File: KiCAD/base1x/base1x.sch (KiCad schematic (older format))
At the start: 41 parts, among them J1 Conn_02x05_Odd_Even, J2 GS3, J3 Conn_02x14_Counter_Clockwise, J4 GS3, J5 Screw_Terminal_01x06, J6 Conn_02x14_Counter_Clockwise, J7 Conn_02x06_Counter_Clockwise, J8 Conn_02x06_Counter_Clockwise, J9 Screw_Terminal_01x08, P1 CONN_01X02, P2 CONN_01X02, P3 CONN_01X02, P4 CONN_01X02, U1 ADS1115

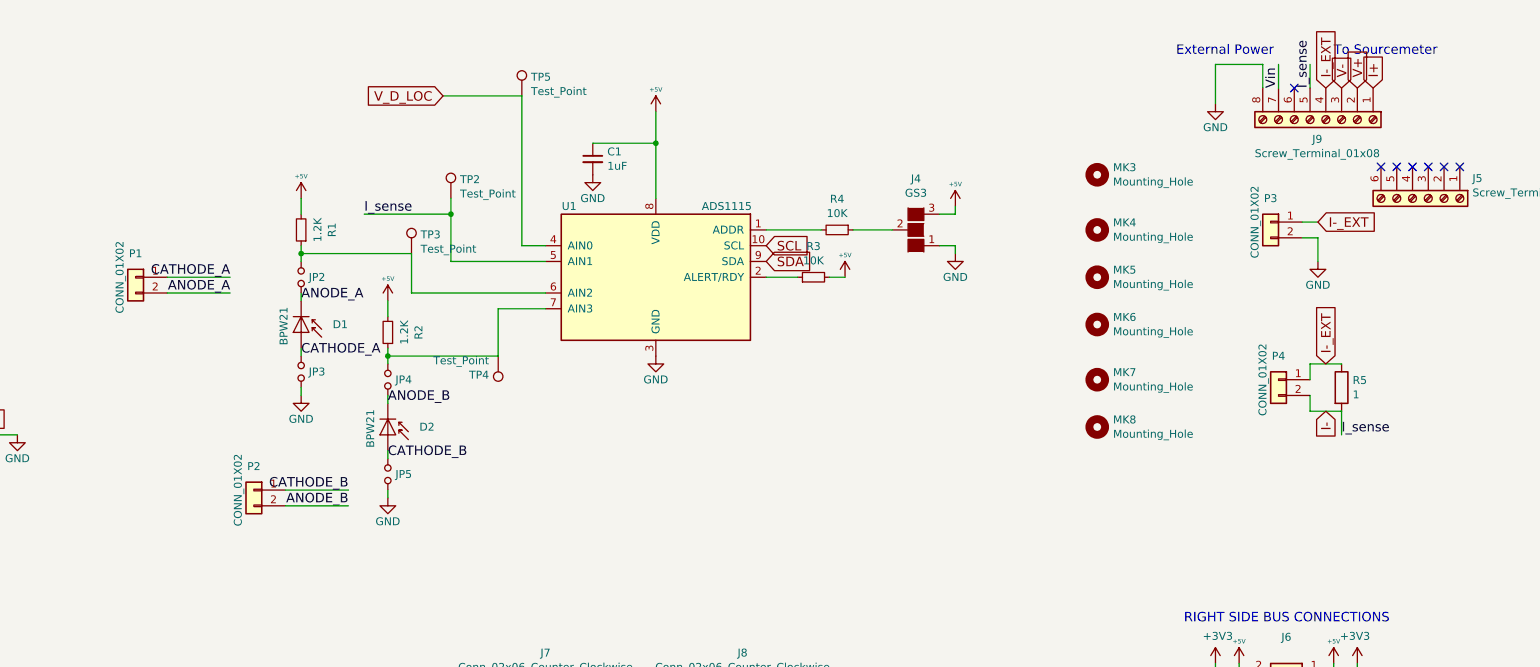
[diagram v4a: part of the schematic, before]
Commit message: rotate connectors on newMux
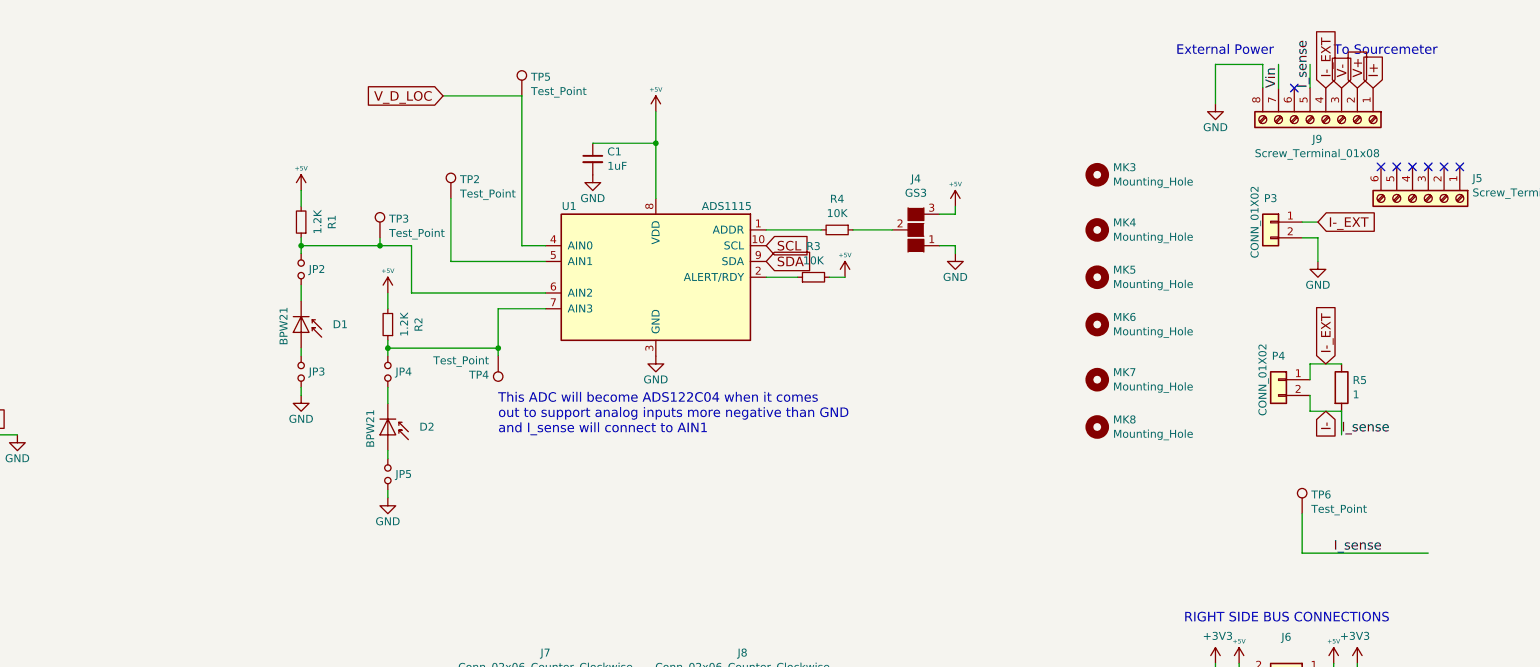
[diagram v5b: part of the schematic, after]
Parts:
- removed P1, P2: CONN_01X02, Pin_Headers:Pin_Header_Straight_1x02_Pitch2.54mm, symbol Conn_01x02
- added TP6: Test_Point, myParts:Test_Point_S1751-46R, symbol Test_Point
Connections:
- net I-: now also TP6.1; no longer TP2.1, U1.5 (AIN1)
- net ANODE_A: no longer names the net of D1.1 (K), JP2.2
- net ANODE_B: no longer names the net of D2.1 (K), JP4.2
- net CATHODE_A: no longer names the net of D1.2 (A), JP3.1
- net CATHODE_B: no longer names the net of D2.2 (A), JP5.1
- new net: TP2.1, U1.5 (AIN1)
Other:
- note added: "This ADC will become ADS122C04 when it comes\nout to support analog inputs more negative than GND\nand I_sense will connect to AIN1"
- moved on the sheet: JP2, JP4, R1, R2, TP3
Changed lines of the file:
@@
 $EndComp
 Wire Wire Line
-	6000 1850 6000 1300
+	6000 1300 6000 1850
 $Comp
 L C_Small C1
@@
 L +5V #PWR013
 U 1 1 59F74573
-P 3750 1850
-F 0 "#PWR013" H 3750 1700 50  0001 C CNN
-F 1 "+5V" H 3750 1990 28  0000 C CNN
-F 2 "" H 3750 1850 50  0000 C CNN
-F 3 "" H 3750 1850 50  0000 C CNN
-	1    3750 1850
+P 3750 1800
+F 0 "#PWR013" H 3750 1650 50  0001 C CNN
+F 1 "+5V" H 3750 1940 28  0000 C CNN
+F 2 "" H 3750 1800 50  0000 C CNN
+F 3 "" H 3750 1800 50  0000 C CNN
+	1    3750 1800
 	1    0    0    -1
 $EndComp
@@
 	1    0    0    -1
 $EndComp
-Text Label 3750 2500 0    60   ~ 0
-ANODE_A
-Text Label 3750 2850 0    60   ~ 0
-CATHODE_A
-$Comp
-L Conn_01x02 P1
-U 1 1 59F745A3
-P 2700 2350
-F 0 "P1" H 2700 2500 50  0000 C CNN
-F 1 "CONN_01X02" V 2800 2350 50  0000 C CNN
-F 2 "Pin_Headers:Pin_Header_Straight_1x02_Pitch2.54mm" H 2700 2350 50  0001 C CNN
-F 3 "" H 2700 2350 50  0000 C CNN
-	1    2700 2350
-	-1   0    0    -1
-$EndComp
-Text Label 3300 2450 2    60   ~ 0
-ANODE_A
-Text Label 3300 2350 2    60   ~ 0
-CATHODE_A
-Wire Wire Line
-	3750 1850 3750 1950
-Wire Wire Line
-	2900 2350 3300 2350
-Wire Wire Line
-	2900 2450 3300 2450
+Wire Wire Line
+	3750 1800 3750 1900
 $Comp
 L R_Small R1
 U 1 1 59F761B7
-P 3750 2050
-F 0 "R1" V 3554 2050 50  0000 C CNN
-F 1 "1.2K" V 3645 2050 50  0000 C CNN
-F 2 "Resistors_SMD:R_0805_HandSoldering" H 3750 2050 50  0001 C CNN
-F 3 "" H 3750 2050 50  0001 C CNN
-	1    3750 2050
+P 3750 2000
+F 0 "R1" V 3554 2000 50  0000 C CNN
+F 1 "1.2K" V 3645 2000 50  0000 C CNN
+F 2 "Resistors_SMD:R_0805_HandSoldering" H 3750 2000 50  0001 C CNN
+F 3 "" H 3750 2000 50  0001 C CNN
+	1    3750 2000
 	-1   0    0    1
 $EndComp
 Wire Wire Line
-	4450 2200 4450 2450
+	4450 2150 4450 2450
 Wire Wire Line
 	4450 2450 5300 2450
@@
 L Jumper_NO_Small JP2
 U 1 1 59F7708F
-P 3750 2350
-F 0 "JP2" V 3750 2398 50  0000 L CNN
-F 1 "Jumper_NO_Small" V 3795 2398 50  0001 L CNN
-F 2 "Connectors:GS2" H 3750 2350 50  0001 C CNN
-F 3 "" H 3750 2350 50  0001 C CNN
-	1    3750 2350
-	0    1    1    0
-$EndComp
-Wire Wire Line
-	3750 2450 3750 2500
-Wire Wire Line
-	3750 2150 3750 2250
-Wire Wire Line
-	4450 2200 3750 2200
-Connection ~ 3750 2200
+P 3750 2300
+F 0 "JP2" V 3750 2348 50  0000 L CNN
+F 1 "Jumper_NO_Small" V 3795 2348 50  0001 L CNN
+F 2 "Connectors:GS2" H 3750 2300 50  0001 C CNN
+F 3 "" H 3750 2300 50  0001 C CNN
+	1    3750 2300
+	0    1    1    0
+$EndComp
+Wire Wire Line
+	3750 2400 3750 2500
+Wire Wire Line
+	3750 2100 3750 2200
+Wire Wire Line
+	4450 2150 3750 2150
+Connection ~ 3750 2150
 $Comp
 L Jumper_NO_Small JP3
@@
 L +5V #PWR016
 U 1 1 59F77B25
-P 4300 2500
-F 0 "#PWR016" H 4300 2350 50  0001 C CNN
-F 1 "+5V" H 4300 2640 28  0000 C CNN
-F 2 "" H 4300 2500 50  0000 C CNN
-F 3 "" H 4300 2500 50  0000 C CNN
-	1    4300 2500
+P 4300 2450
+F 0 "#PWR016" H 4300 2300 50  0001 C CNN
+F 1 "+5V" H 4300 2590 28  0000 C CNN
+F 2 "" H 4300 2450 50  0000 C CNN
+F 3 "" H 4300 2450 50  0000 C CNN
+	1    4300 2450
 	1    0    0    -1
 $EndComp
@@
 	1    0    0    -1
 $EndComp
-Text Label 4300 3150 0    60   ~ 0
-ANODE_B
-Text Label 4300 3500 0    60   ~ 0
-CATHODE_B
-Wire Wire Line
-	4300 2500 4300 2600
+Wire Wire Line
+	4300 2450 4300 2550
 $Comp
 L R_Small R2
 U 1 1 59F77B34
-P 4300 2700
-F 0 "R2" V 4104 2700 50  0000 C CNN
-F 1 "1.2K" V 4195 2700 50  0000 C CNN
-F 2 "Resistors_SMD:R_0805_HandSoldering" H 4300 2700 50  0001 C CNN
-F 3 "" H 4300 2700 50  0001 C CNN
-	1    4300 2700
+P 4300 2650
+F 0 "R2" V 4104 2650 50  0000 C CNN
+F 1 "1.2K" V 4195 2650 50  0000 C CNN
+F 2 "Resistors_SMD:R_0805_HandSoldering" H 4300 2650 50  0001 C CNN
+F 3 "" H 4300 2650 50  0001 C CNN
+	1    4300 2650
 	-1   0    0    1
 $EndComp
@@
 L Jumper_NO_Small JP4
 U 1 1 59F77B3B
-P 4300 3000
-F 0 "JP4" V 4300 3048 50  0000 L CNN
-F 1 "Jumper_NO_Small" V 4345 3048 50  0001 L CNN
-F 2 "Connectors:GS2" H 4300 3000 50  0001 C CNN
-F 3 "" H 4300 3000 50  0001 C CNN
-	1    4300 3000
-	0    1    1    0
-$EndComp
-Wire Wire Line
-	4300 3100 4300 3150
-Wire Wire Line
-	4300 2800 4300 2900
-Wire Wire Line
-	5000 2850 4300 2850
-Connection ~ 4300 2850
-$Comp
-L Jumper_NO_Small JP5
-U 1 1 59F77B46
-P 4300 3600
-F 0 "JP5" V 4300 3648 50  0000 L CNN
-F 1 "Jumper_NO_Small" V 4345 3648 50  0001 L CNN
-F 2 "Connectors:GS2" H 4300 3600 50  0001 C CNN
-F 3 "" H 4300 3600 50  0001 C CNN
-	1    4300 3600
-	0    1    1    0
-$EndComp
+P 4300 2950
+F 0 "JP4" V 4300 2998 50  0000 L CNN
+F 1 "Jumper_NO_Small" V 4345 2998 50  0001 L CNN
+F 2 "Connectors:GS2" H 4300 2950 50  0001 C CNN
+F 3 "" H 4300 2950 50  0001 C CNN
+	1    4300 2950
+	0    1    1    0
+$EndComp
+Wire Wire Line
+	4300 3050 4300 3150
+Wire Wire Line
+	4300 2750 4300 2850
+Wire Wire Line
+	5000 2800 4300 2800
+Connection ~ 4300 2800
 Wire Wire Line
 	4300 3450 4300 3500
@@
 	4300 3700 4300 3750
 Wire Wire Line
-	5000 2850 5000 2550
+	5000 2550 5000 2850
 Wire Wire Line
 	5000 2550 5300 2550
-$Comp
-L Conn_01x02 P2
-U 1 1 59F77FAB
-P 3450 3700
-F 0 "P2" H 3450 3850 50  0000 C CNN
-F 1 "CONN_01X02" V 3550 3700 50  0000 C CNN
-F 2 "Pin_Headers:Pin_Header_Straight_1x02_Pitch2.54mm" H 3450 3700 50  0001 C CNN
-F 3 "" H 3450 3700 50  0000 C CNN
-	1    3450 3700
-	-1   0    0    -1
-$EndComp
-Text Label 4050 3800 2    60   ~ 0
-ANODE_B
-Text Label 4050 3700 2    60   ~ 0
-CATHODE_B
-Wire Wire Line
-	3650 3700 4050 3700
-Wire Wire Line
-	3650 3800 4050 3800
 $Comp
 L GS3 J2
@@
 L Test_Point TP3
 U 1 1 5A3700D5
-P 4450 2200
-F 0 "TP3" H 4508 2320 50  0000 L CNN
-F 1 "Test_Point" H 4508 2229 50  0000 L CNN
-F 2 "myParts:Test_Point_S1751-46R" H 4650 2200 50  0001 C CNN
-F 3 "" H 4650 2200 50  0001 C CNN
-	1    4450 2200
+P 4250 2100
+F 0 "TP3" H 4308 2220 50  0000 L CNN
+F 1 "Test_Point" H 4308 2129 50  0000 L CNN
+F 2 "myParts:Test_Point_S1751-46R" H 4450 2100 50  0001 C CNN
+F 3 "" H 4450 2100 50  0001 C CNN
+	1    4250 2100
 	1    0    0    -1
 $EndComp
@@
 	-1   0    0    1
 $EndComp
-Wire Wire Line
-	4700 1950 4150 1950
-Connection ~ 4700 1950
-Text Label 4150 1950 0    60   ~ 0
-I_sense
 Text GLabel 4650 1200 0    60   Input ~ 0
 V_D_LOC
@@
 	1    0    0    -1
 $EndComp
+Text Notes 5000 3350 0    60   ~ 0
+This ADC will become ADS122C04 when it comes\nout to support analog inputs more negative than GND\nand I_sense will connect to AIN1
+$Comp
+L Test_Point TP6
+U 1 1 5A58BDB1
+P 10100 3850
+F 0 "TP6" H 10158 3970 50  0000 L CNN
+F 1 "Test_Point" H 10158 3879 50  0000 L CNN
+F 2 "myParts:Test_Point_S1751-46R" H 10300 3850 50  0001 C CNN
+F 3 "" H 10300 3850 50  0001 C CNN
+	1    10100 3850
+	1    0    0    -1
+$EndComp
+Wire Wire Line
+	10100 3850 10100 4100
+Wire Wire Line
+	10100 4100 10900 4100
+Text Label 10300 4100 0    60   ~ 0
+I_sense
+$Comp
+L Jumper_NO_Small JP5
+U 1 1 59F77B46
+P 4300 3600
+F 0 "JP5" V 4300 3648 50  0000 L CNN
+F 1 "Jumper_NO_Small" V 4345 3648 50  0001 L CNN
+F 2 "Connectors:GS2" H 4300 3600 50  0001 C CNN
+F 3 "" H 4300 3600 50  0001 C CNN
+	1    4300 3600
+	0    1    1    0
+$EndComp
+Wire Wire Line
+	4250 2100 4250 2150
+Connection ~ 4250 2150
+Connection ~ 5000 2800
 $EndSCHEMATC

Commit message: rotate connectors on base1x
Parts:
- C1: symbol C_Small -> device:C_Small
- D1, D2: symbol D_Photo -> device:D_Photo
- J1: symbol Conn_02x05_Odd_Even -> Connector:Conn_02x05_Odd_Even
- J2, J4: symbol GS3 -> Connector:GS3
- J3, J6: symbol Conn_02x14_Odd_Even -> Connector:Conn_02x14_Odd_Even
- J5: symbol Screw_Terminal_01x06 -> Connector:Screw_Terminal_01x06
- J7, J8: symbol Conn_02x06_Counter_Clockwise -> Connector:Conn_02x06_Odd_Even
- J9: symbol Screw_Terminal_01x08 -> Connector:Screw_Terminal_01x08
- JP2, JP3, JP4, JP5, JP6: symbol Jumper_NO_Small -> device:Jumper_NO_Small
- L1: symbol GREY@CHRISTOFORO.NET -> myParts:GREY@CHRISTOFORO.NET
- MK1, MK2: symbol Mounting_Hole_PAD -> Mechanical:Mounting_Hole_PAD
- MK3, MK4, MK5, MK6, MK7, MK8: symbol Mounting_Hole -> Mechanical:Mounting_Hole
- P3, P4: symbol Conn_01x02 -> Connector:Conn_01x02
- R1, R2, R3, R4: symbol R_Small -> device:R_Small
- R5: symbol R -> device:R
- TP1, TP2, TP3, TP4, TP5, TP6: symbol Test_Point -> Connector:Test_Point
- U1: symbol ADS1115 -> myParts:ADS1115
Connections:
- wire segments 93 -> 99
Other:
- note added: "Current Sense Resistor"
- note added: "Legacy connector for posterity"
- moved on the sheet: J5

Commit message: update farnell codes
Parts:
- D1, D2: farnellCode (none) -> 1045427
- J1: farnellCode (none) -> 2055711
- R1, R2: farnellCode (none) -> 2073370
- R3, R4: farnellCode (none) -> 2073607
- TP1, TP2, TP3, TP4, TP5, TP6: farnellCode (none) -> 2293786
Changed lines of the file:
@@
 F 2 "Pin_Headers:Pin_Header_Angled_2x05_Pitch2.54mm" H 1250 3350 50  0001 C CNN
 F 3 "" H 1250 3350 50  0001 C CNN
+F 4 "2055711" H 0   0   50  0001 C CNN "farnellCode"
 	1    1250 3350
 	1    0    0    -1
@@
 F 2 "Resistors_SMD:R_0805_HandSoldering" H 7150 2050 50  0001 C CNN
 F 3 "" H 7150 2050 50  0001 C CNN
+F 4 "2073607" H 0   0   50  0001 C CNN "farnellCode"
 	1    7150 2050
 	0    1    1    0
@@
 F 2 "Resistors_SMD:R_0805_HandSoldering" H 7000 2350 50  0001 C CNN
 F 3 "" H 7000 2350 50  0001 C CNN
+F 4 "2073607" H 0   0   50  0001 C CNN "farnellCode"
 	1    7000 2350
 	0    -1   -1   0
@@
 F 2 "myParts:BPW21" H 3700 2700 50  0001 C CNN
 F 3 "" H 3700 2700 50  0000 C CNN
+F 4 "1045427" H 0   0   50  0001 C CNN "farnellCode"
 	1    3750 2700
 	0    1    1    0
@@
 F 2 "Resistors_SMD:R_0805_HandSoldering" H 3750 2000 50  0001 C CNN
 F 3 "" H 3750 2000 50  0001 C CNN
+F 4 "2073370" H 0   0   50  0001 C CNN "farnellCode"
 	1    3750 2000
 	-1   0    0    1
@@
 F 2 "myParts:BPW21" H 4250 3350 50  0001 C CNN
 F 3 "" H 4250 3350 50  0000 C CNN
+F 4 "1045427" H 0   0   50  0001 C CNN "farnellCode"
 	1    4300 3350
 	0    1    1    0
@@
 F 2 "Resistors_SMD:R_0805_HandSoldering" H 4300 2650 50  0001 C CNN
 F 3 "" H 4300 2650 50  0001 C CNN
+F 4 "2073370" H 0   0   50  0001 C CNN "farnellCode"
 	1    4300 2650
 	-1   0    0    1
@@
 F 2 "myParts:Test_Point_S1751-46R" H 5850 6300 50  0001 C CNN
 F 3 "" H 5850 6300 50  0001 C CNN
+F 4 "2293786" H 0   0   50  0001 C CNN "farnellCode"
 	1    5650 6300
 	1    0    0    -1
@@
 F 2 "myParts:Test_Point_S1751-46R" H 4900 1850 50  0001 C CNN
 F 3 "" H 4900 1850 50  0001 C CNN
+F 4 "2293786" H 0   0   50  0001 C CNN "farnellCode"
 	1    4700 1850
 	1    0    0    -1
@@
 F 2 "myParts:Test_Point_S1751-46R" H 4450 2100 50  0001 C CNN
 F 3 "" H 4450 2100 50  0001 C CNN
+F 4 "2293786" H 0   0   50  0001 C CNN "farnellCode"
 	1    4250 2100
 	1    0    0    -1
@@
 F 2 "myParts:Test_Point_S1751-46R" H 5200 2850 50  0001 C CNN
 F 3 "" H 5200 2850 50  0001 C CNN
+F 4 "2293786" H 0   0   50  0001 C CNN "farnellCode"
 	1    5000 2850
 	-1   0    0    1
@@
 F 2 "myParts:Test_Point_S1751-46R" H 5350 1200 50  0001 C CNN
 F 3 "" H 5350 1200 50  0001 C CNN
+F 4 "2293786" H 0   0   50  0001 C CNN "farnellCode"
 	1    5150 1200
 	1    0    0    -1
@@
 F 2 "myParts:Test_Point_S1751-46R" H 10300 3850 50  0001 C CNN
 F 3 "" H 10300 3850 50  0001 C CNN
+F 4 "2293786" H 0   0   50  0001 C CNN "farnellCode"
 	1    10100 3850
 	1    0    0    -1

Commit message: upgrade syms and layouts to kicad5
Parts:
- removed J5: Screw_Terminal_01x06, Connectors_Phoenix:PhoenixContact_MC-GF_06x3.50mm_Angled_ThreadedFlange_MountHole, symbol Connector:Screw_Terminal_01x06
- C1: footprint Capacitors_SMD:C_0805_HandSoldering -> Capacitor_SMD:C_1206_3216Metric; symbol device:C_Small -> Device:C_Small
- D1, D2: symbol device:D_Photo -> Device:D_Photo
- J1: footprint Pin_Headers:Pin_Header_Angled_2x05_Pitch2.54mm -> Connector_IDC:IDC-Header_2x05_P2.54mm_Horizontal; symbol Connector:Conn_02x05_Odd_Even -> Connector_Generic:Conn_02x05_Odd_Even; farnellCode 2055711 -> 2215290
- J2, J4: footprint Connectors:GS3 -> Jumper:SolderJumper-3_P1.3mm_Open_RoundedPad1.0x1.5mm_NumberLabels; symbol Connector:GS3 -> Jumper:SolderJumper_3_Open
- J3, J6: footprint Socket_Strips:Socket_Strip_Straight_2x14_Pitch2.54mm -> Connector_PinSocket_2.54mm:PinSocket_2x14_P2.54mm_Vertical; symbol Connector:Conn_02x14_Odd_Even -> Connector_Generic:Conn_02x14_Odd_Even
- J7, J8: footprint Socket_Strips:Socket_Strip_Straight_2x06_Pitch2.54mm -> Connector_PinHeader_2.54mm:PinHeader_2x06_P2.54mm_Vertical; symbol Connector:Conn_02x06_Odd_Even -> Connector_Generic:Conn_02x06_Odd_Even
- J9: footprint Connectors_Phoenix:PhoenixContact_MC-GF_08x3.50mm_Angled_ThreadedFlange_MountHole -> Connector_Phoenix_MC:PhoenixContact_MC_1,5_8-GF-3.5_1x08_P3.50mm_Horizontal_ThreadedFlange_MountHole; symbol Connector:Screw_Terminal_01x08 -> Connector_Specialized:Screw_Terminal_01x08
- JP2, JP3, JP4, JP5, JP6: footprint Connectors:GS2 -> Jumper:SolderJumper-2_P1.3mm_Open_RoundedPad1.0x1.5mm; symbol device:Jumper_NO_Small -> Device:Jumper_NO_Small
- MK1, MK2: footprint Mounting_Holes:MountingHole_2.2mm_M2_Pad -> MountingHole:MountingHole_2.2mm_M2_Pad
- MK3, MK4: footprint Mounting_Holes:MountingHole_6mm -> MountingHole:MountingHole_6mm
- MK5, MK7, MK8: footprint Mounting_Holes:MountingHole_3.2mm_M3 -> MountingHole:MountingHole_3.2mm_M3
- MK6: footprint Mounting_Holes:MountingHole_4.3mm_M4 -> MountingHole:MountingHole_4.3mm_M4
- P3, P4: footprint Pin_Headers:Pin_Header_Straight_1x02_Pitch2.54mm -> Connector_PinHeader_2.54mm:PinHeader_1x02_P2.54mm_Vertical; symbol Connector:Conn_01x02 -> Connector_Generic:Conn_01x02
- R1, R2, R3, R4: footprint Resistors_SMD:R_0805_HandSoldering -> Resistor_SMD:R_1206_3216Metric; symbol device:R_Small -> Device:R_Small
- R5: footprint Resistors_SMD:R_2512_HandSoldering -> Resistor_SMD:R_2512_6332Metric; symbol device:R -> Device:R
- TP1, TP2, TP3, TP4, TP5, TP6: symbol Connector:Test_Point -> Connector_Specialized:Test_Point
- U1: footprint Housings_SSOP:MSOP-10_3x3mm_Pitch0.5mm -> Package_SO:MSOP-10_3x3mm_P0.5mm
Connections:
- no-connect marks 41 -> 35
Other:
- note removed: "Legacy connector for posterity"
